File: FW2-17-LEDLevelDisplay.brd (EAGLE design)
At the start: 125 x 34 mm, 60 parts, among them Q1 BC557, Q10 BC547, Q11 BC547, Q2 BC547, Q3 BC547, Q4 BC547, Q5 BC547, Q6 BC547, Q7 BC547, Q8 BC547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

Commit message: Reduced size of diode footprints; fixed part values
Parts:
- D1, D10, D2, D3, D4, D5, D6, D7, D8, D9: value 1N914 -> 1N4148; device freetronics-master-v1.1:DIODE-1N4148 -> freetronics-master-v1.1:DIODE-1N914
- JP1: value M01PTH -> IN+
- JP2: value M01PTH -> IN-
- JP3: value M01PTH -> PWR+
- JP4: value M01PTH -> PWR-
- moved D10 14.0 mm to (111.8, 3.81)
- moved D9 11.4 mm to (104.1, 3.81)
- moved D8 8.89 mm to (96.5, 3.81)
- moved D2 6.35 mm to (50.8, 3.81)
- moved D7 6.35 mm to (88.9, 3.81)
- moved D3 3.81 mm to (58.4, 3.81)
- moved D6 3.81 mm to (81.3, 3.81)
- moved R1 2.54 mm to (7.62, 19.1)
- moved D4 1.27 mm to (66.0, 3.81)
- moved D5 1.27 mm to (73.7, 3.81)
- moved D1 1.27 mm to (29.2, 29.2)
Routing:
- net N$1: track 18.5 -> 3.81 mm
- net N$30: track 17.8 -> 8.15 mm
- net N$29: track 15.3 -> 8.15 mm
- net N$13: track 21.7 -> 26.5 mm
- net N$28: track 12.8 -> 8.15 mm
- net N$10: track 10.4 -> 8.15 mm
- net N$26: track 6.43 -> 8.15 mm
- net N$27: track 6.43 -> 8.15 mm
- net N$6: track 186.8 -> 188.3 mm
- net N$47: track 5.08 -> 6.13 mm
- net N$46: track 18.6 -> 19.6 mm
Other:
- board text added: "(c) 2016 Freetronics Pty Ltd"
- board text added: "+"
- board text removed: "(c) 2016 Freetronics"

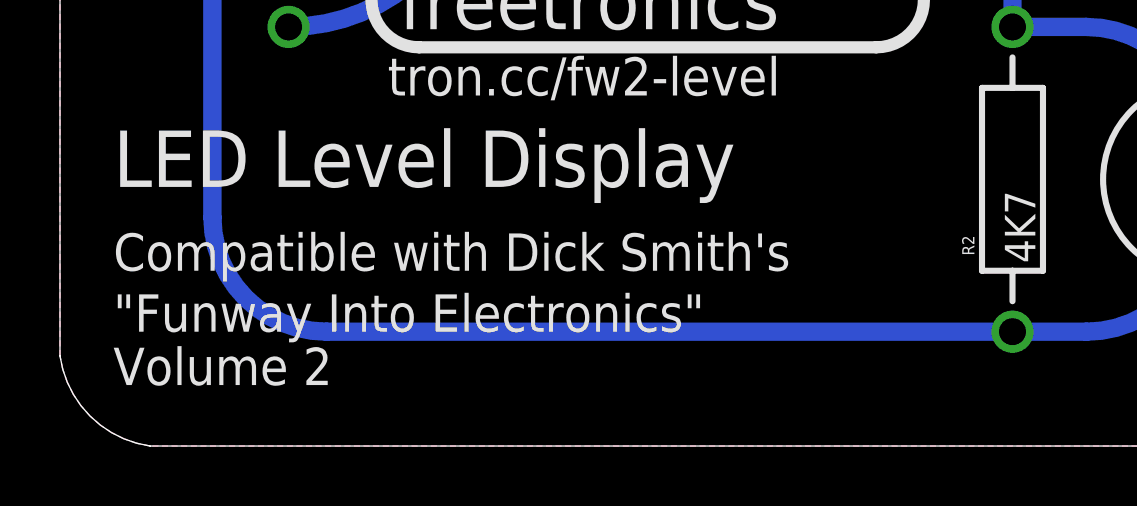
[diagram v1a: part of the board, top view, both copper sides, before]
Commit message: Updated silkscreen and labels
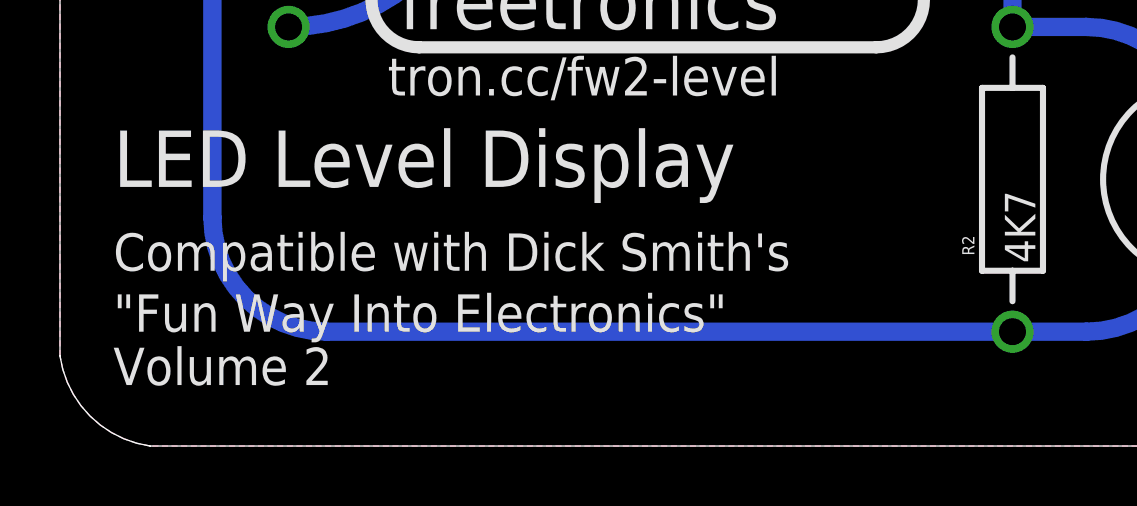
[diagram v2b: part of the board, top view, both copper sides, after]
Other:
- board text added: ""Fun Way Into Electronics""
- board text removed: ""Funway Into Electronics""
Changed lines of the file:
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@@
 <text x="29.3" y="15.412" size="1.27" layer="22" font="vector" ratio="16" rot="SMR0">SKU: FW2LEVEL</text>
 <text x="1.778" y="5.842" size="1.2446" layer="21" font="vector" ratio="15">Compatible with Dick Smith's</text>
-<text x="1.778" y="3.81" size="1.2446" layer="21" font="vector" ratio="15">"Funway Into Electronics"</text>
+<text x="1.778" y="3.81" size="1.2446" layer="21" font="vector" ratio="15">"Fun Way Into Electronics"</text>
 <wire x1="121.158" y1="19.05" x2="123.19" y2="19.05" width="0.4064" layer="21"/>
 <wire x1="121.158" y1="24.13" x2="123.19" y2="24.13" width="0.4064" layer="21"/>

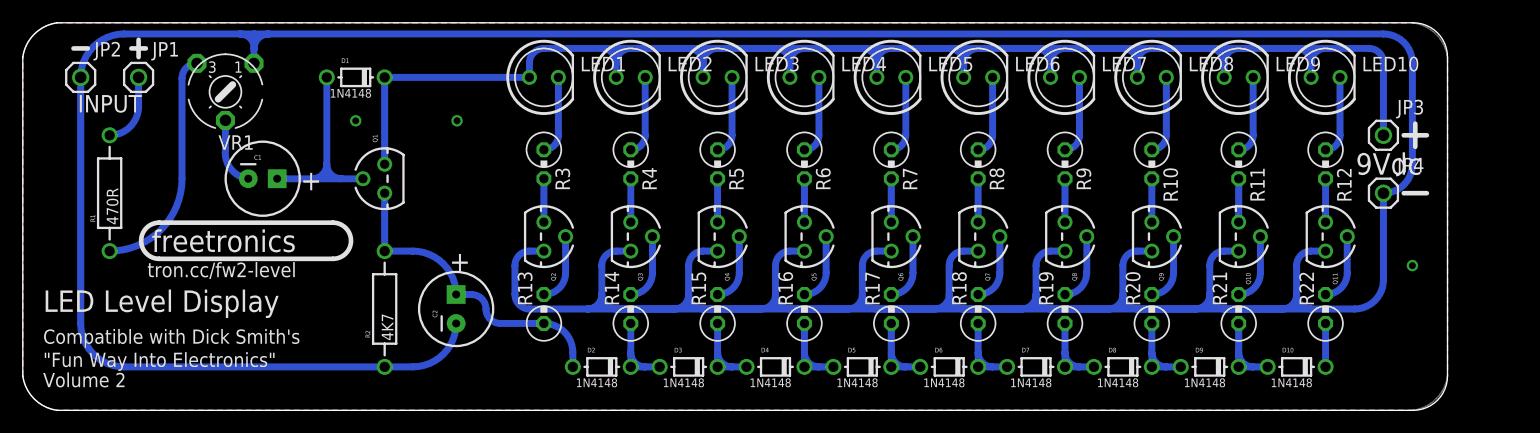
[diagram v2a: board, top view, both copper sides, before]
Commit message: Increased pad size; improved silkscreen
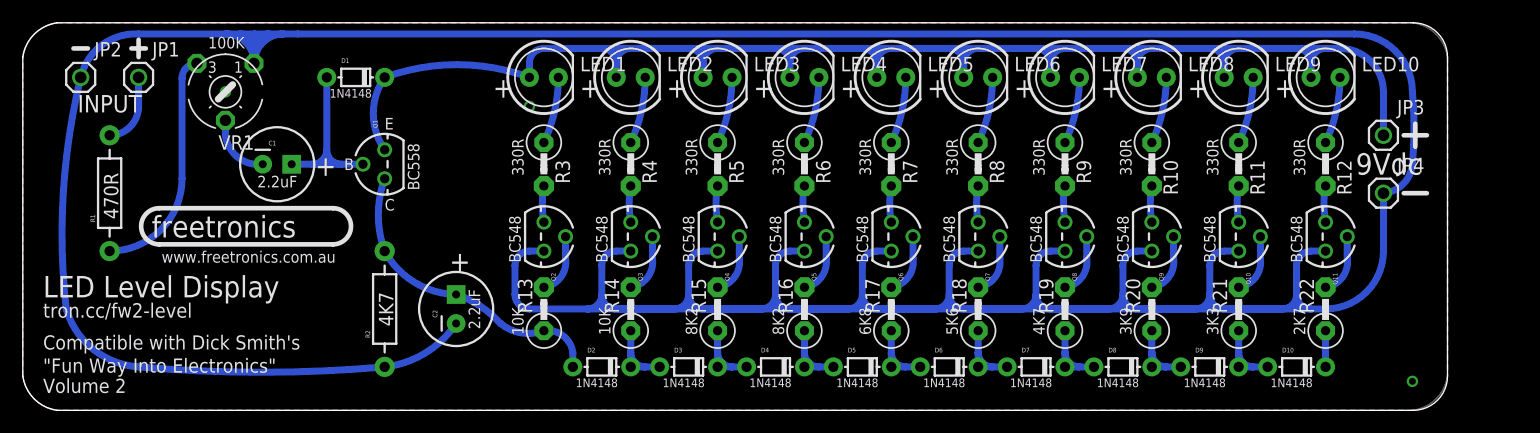
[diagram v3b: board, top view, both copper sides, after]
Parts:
- D1, D10, D2, D3, D4, D5, D6, D7, D8, D9: device freetronics-master-v1.1:DIODE-1N914 -> freetronics-master-v1.1:DIODE-1N914L
- LED1, LED10, LED2, LED3, LED4, LED5, LED6, LED7, LED8, LED9: device freetronics-master-v1.1:LED5MM -> freetronics-master-v1.1:LED5MMLARGE
- R1, R2: device freetronics:FREETRONICS_AXIAL-0.4 -> freetronics:AXIAL-0.4-LARGE
- R10, R11, R12, R13, R14, R15, R16, R17, R18, R19, R20, R21, R22, R3, R4, R5, R6, R7, R8, R9: device resistor:0309V -> freetronics-jon:0309VW
- moved C1 1.80 mm to (22.3, 21.6)
- moved Q1 1.27 mm to (31.8, 21.6)
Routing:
- net N$15: track 410.3 -> 413.9 mm
- net N$6: track 188.3 -> 185.6 mm
- net N$43: track 18.7 -> 16.2 mm
- net N$21: track 6.88 -> 5.85 mm
- net N$4: track 6.88 -> 5.85 mm
- net N$8: track 6.88 -> 5.85 mm
- net N$42: track 6.88 -> 5.85 mm
- net N$40: track 6.88 -> 5.85 mm
- net N$38: track 6.88 -> 5.85 mm
- net N$36: track 6.88 -> 5.85 mm
- net N$19: track 6.88 -> 5.85 mm
- net N$17: track 6.88 -> 5.85 mm
- net N$11: track 6.88 -> 5.85 mm
- net N$5: track 5.87 -> 5.08 mm
- net N$33: track 5.87 -> 5.08 mm
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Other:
- board text added: "100K"
- board text added: "10K"
- board text added: "2.2uF"
- board text added: "2K7"
- board text added: "330R"
- board text added: "3K3"
- board text added: "3K9"
- board text added: "4K7"
- board text added: "5K6"
- board text added: "6K8"
- board text added: "8K2"
- board text added: "B"
- board text added: "BC548"
- board text added: "BC558"
- board text added: "C"
- board text added: "E"
- board text added: "v1.0"
- board text added: "www.freetronics.com.au"
